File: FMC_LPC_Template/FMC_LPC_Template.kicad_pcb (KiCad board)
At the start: 2 copper layers, 78.8 x 69 mm, 5 parts, among them J1 Samtec_ASP-134602-01

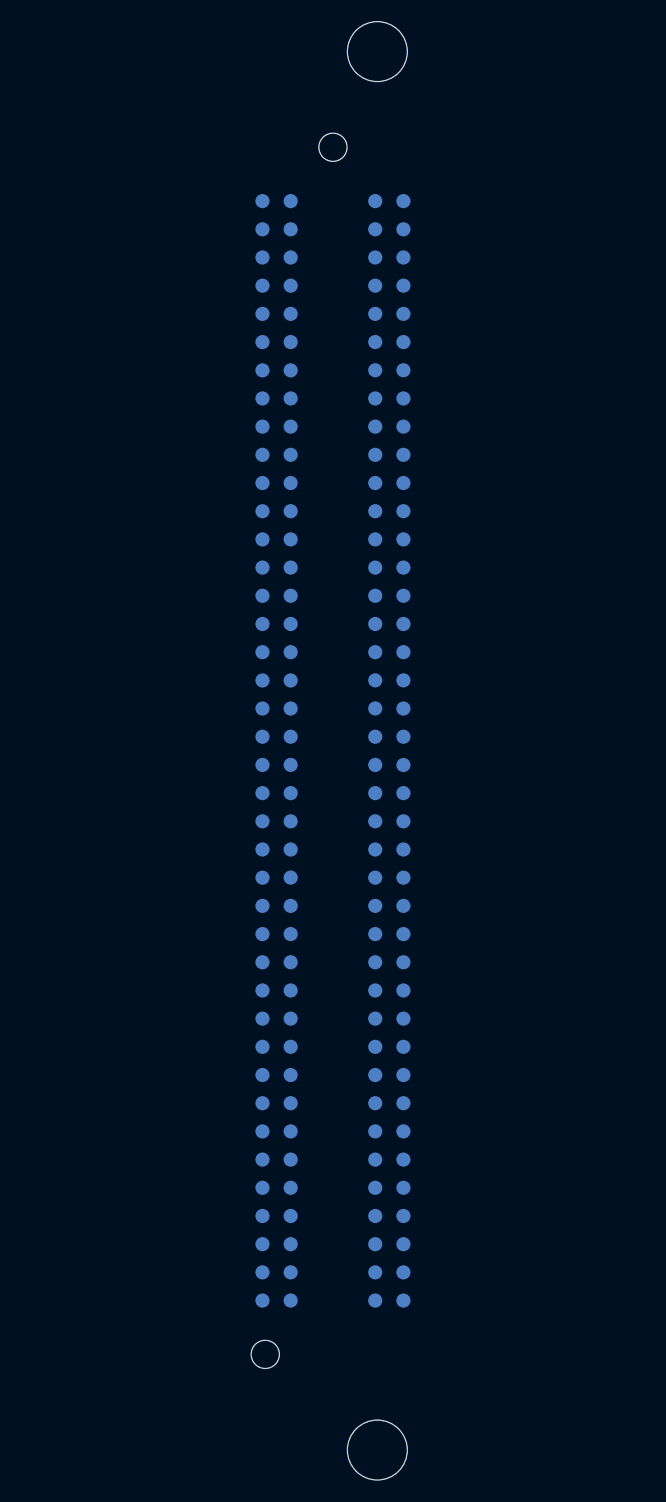
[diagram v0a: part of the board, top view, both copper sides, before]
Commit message: bugfix: Fix for FMC orientation.
When originally laying out the template I used a mirror image of the
FMCHUB expansion board as a reference and totally missed the fact it was
180 deg out of alignment.  This commit simply rotates the connector
about its origin.
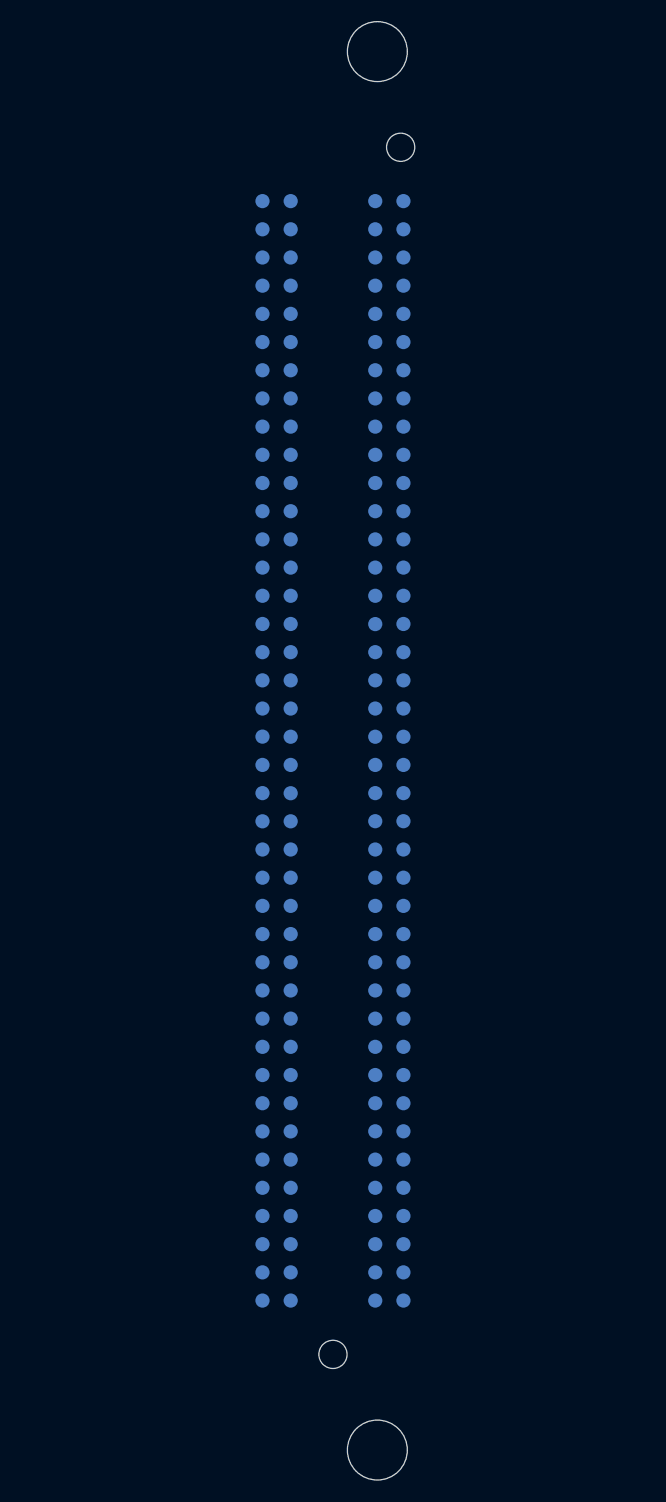
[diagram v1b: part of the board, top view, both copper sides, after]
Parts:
- turned J1 to 0 degrees
